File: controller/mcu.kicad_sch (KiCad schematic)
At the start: 20 parts, among them U1 AP2112K-3.3, U2 RP2040, U3 W25Q128JVS, Y1 Crystal

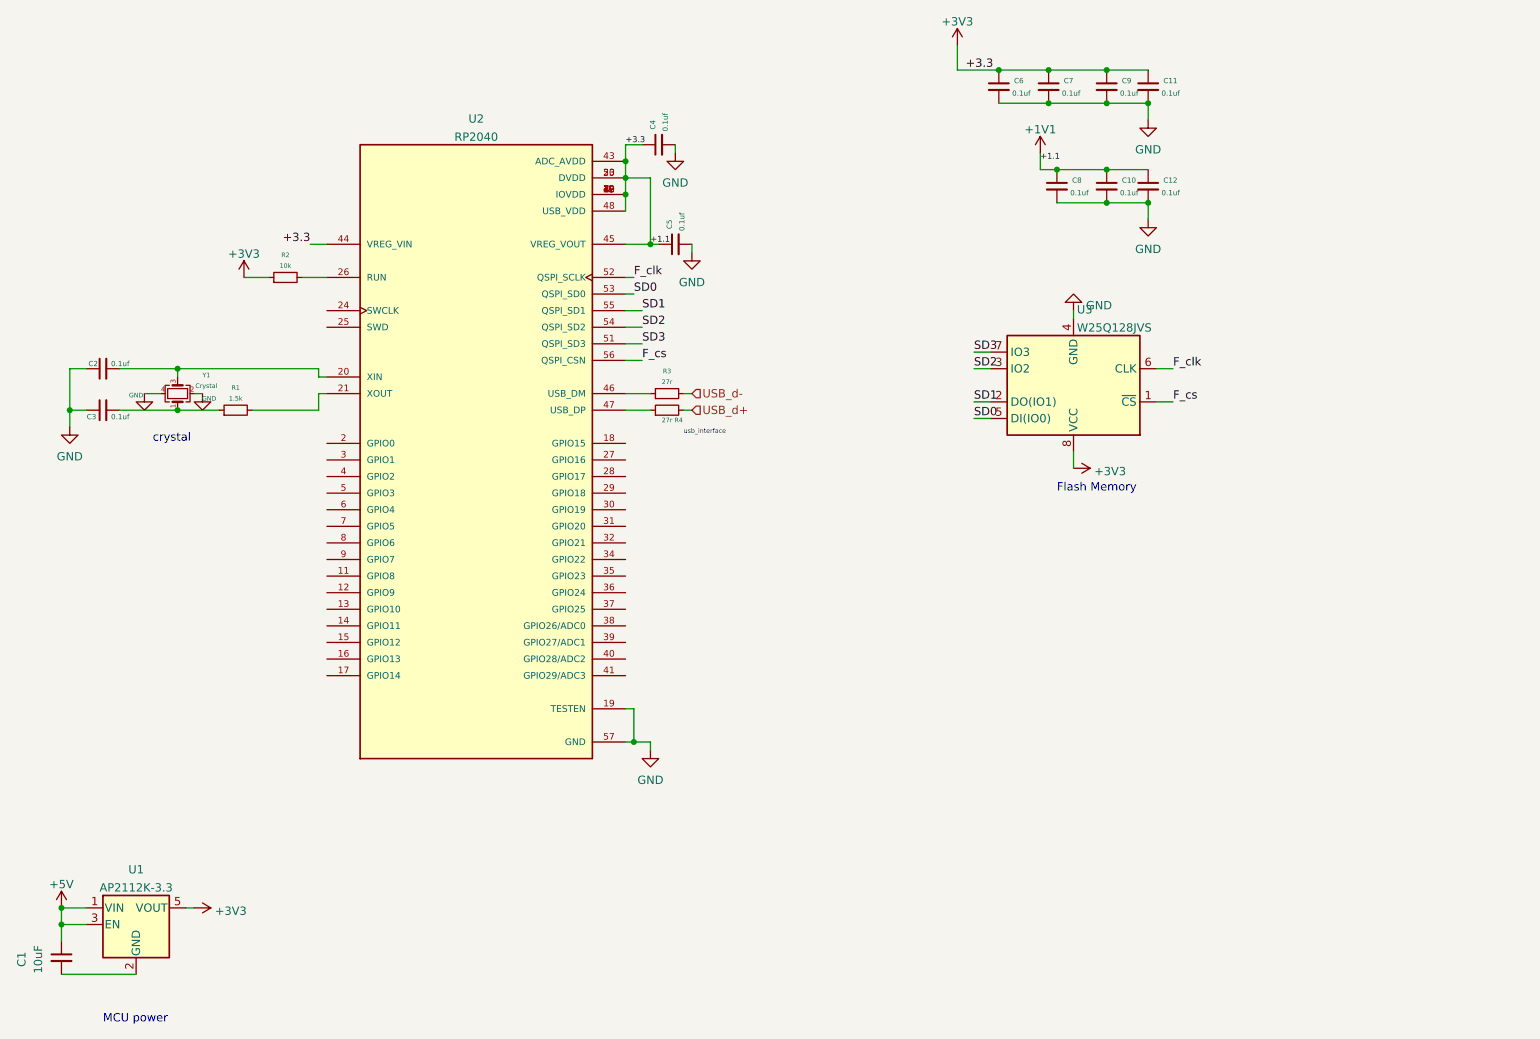
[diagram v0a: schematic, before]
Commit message: Controller Complete
Completed Controller Section
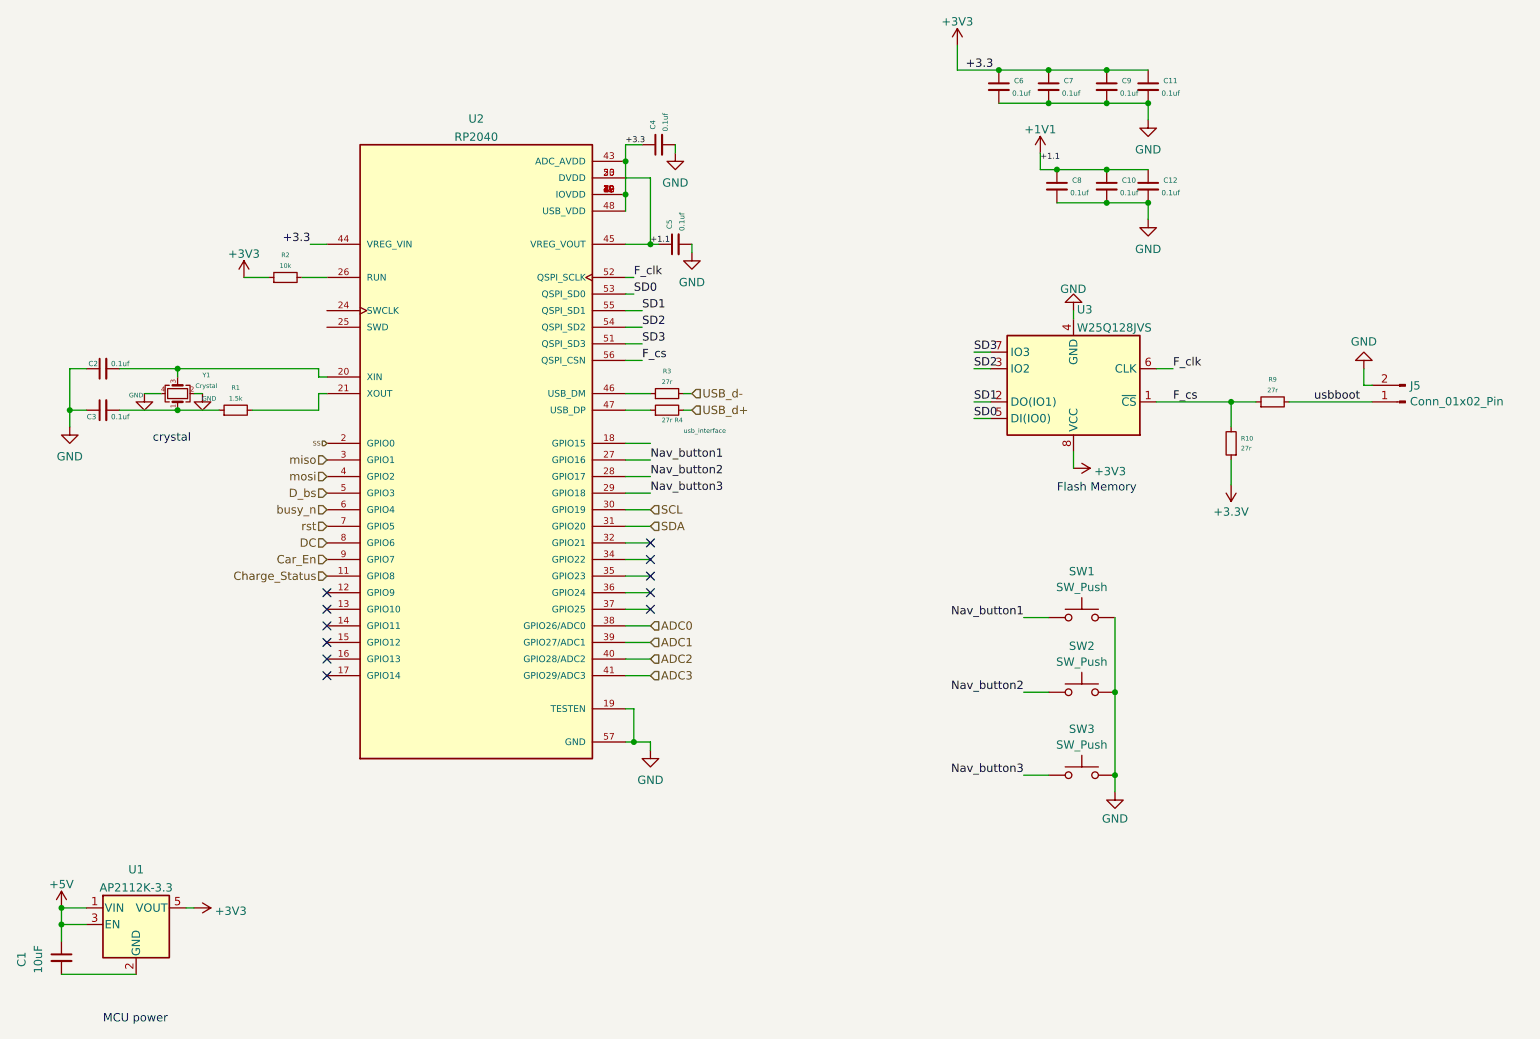
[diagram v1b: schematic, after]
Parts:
- added J5: Conn_01x02_Pin, symbol Connector:Conn_01x02_Pin
- added R10, R9: 27r, symbol Device:R_Small
- added SW1, SW2, SW3: SW_Push, symbol Switch:SW_Push
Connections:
- net +1V1: no longer C11.1, C4.1, C6.1, C7.1, C9.1, R2.1, U1.5 (VOUT), U2.1 (IOVDD), U2.10 (IOVDD), U2.22 (IOVDD), U2.33 (IOVDD), U2.42 (IOVDD), U2.43 (ADC_AVDD), U2.44 (VREG_VIN), U2.48 (USB_VDD), U2.49 (IOVDD), U3.8 (VCC)
- net F_cs: now also R10.2, R9.1
- net GND: now also J5.2 (Pin_2), SW1.2, SW2.2, SW3.2
- net Charge_Status: now reaches U2.11 (GPIO8)
- net SS: now reaches U2.2 (GPIO0)
- net Nav_button1: now reaches U2.27 (GPIO16)
- net Nav_button1: now also SW1.1
- net Nav_button2: now reaches U2.28 (GPIO17)
- net Nav_button2: now also SW2.1
- net Nav_button3: now reaches U2.29 (GPIO18)
- net Nav_button3: now also SW3.1
- net miso: now reaches U2.3 (GPIO1)
- net SCL: now reaches U2.30 (GPIO19)
- net SDA: now reaches U2.31 (GPIO20)
- net ADC0: now reaches U2.38 (GPIO26/ADC0)
- net ADC1: now reaches U2.39 (GPIO27/ADC1)
- net mosi: now reaches U2.4 (GPIO2)
- net ADC2: now reaches U2.40 (GPIO28/ADC2)
- net ADC3: now reaches U2.41 (GPIO29/ADC3)
- net D_bs: now reaches U2.5 (GPIO3)
- net busy_n: now reaches U2.6 (GPIO4)
- net rst: now reaches U2.7 (GPIO5)
- net DC: now reaches U2.8 (GPIO6)
- net Car_En: now reaches U2.9 (GPIO7)
- new net +3.3V: R10.1
- new net +3V3: C11.1, C4.1, C6.1, C7.1, C9.1, R2.1, U1.5 (VOUT), U2.1 (IOVDD), U2.10 (IOVDD), U2.22 (IOVDD), U2.33 (IOVDD), U2.42 (IOVDD), U2.43 (ADC_AVDD), U2.44 (VREG_VIN), U2.48 (USB_VDD), U2.49 (IOVDD), U3.8 (VCC)
- new net usbboot: J5.1 (Pin_1), R9.2
- no-connect marks 0 -> 11
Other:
- company: (none) -> Voltaworks
